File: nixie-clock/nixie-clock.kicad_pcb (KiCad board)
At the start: 2 copper layers, 184 x 105 mm, 61 parts, among them J1 Barrel_Jack_Switch, J2 Conn_01x08, J3 Conn_01x06, J4 AVR-ISP-6, SW1 SW_Push, SW2 SW_Push, SW3 SW_Push, SW4 SW_Push, U1 NCH6100HV, U10 74HC595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

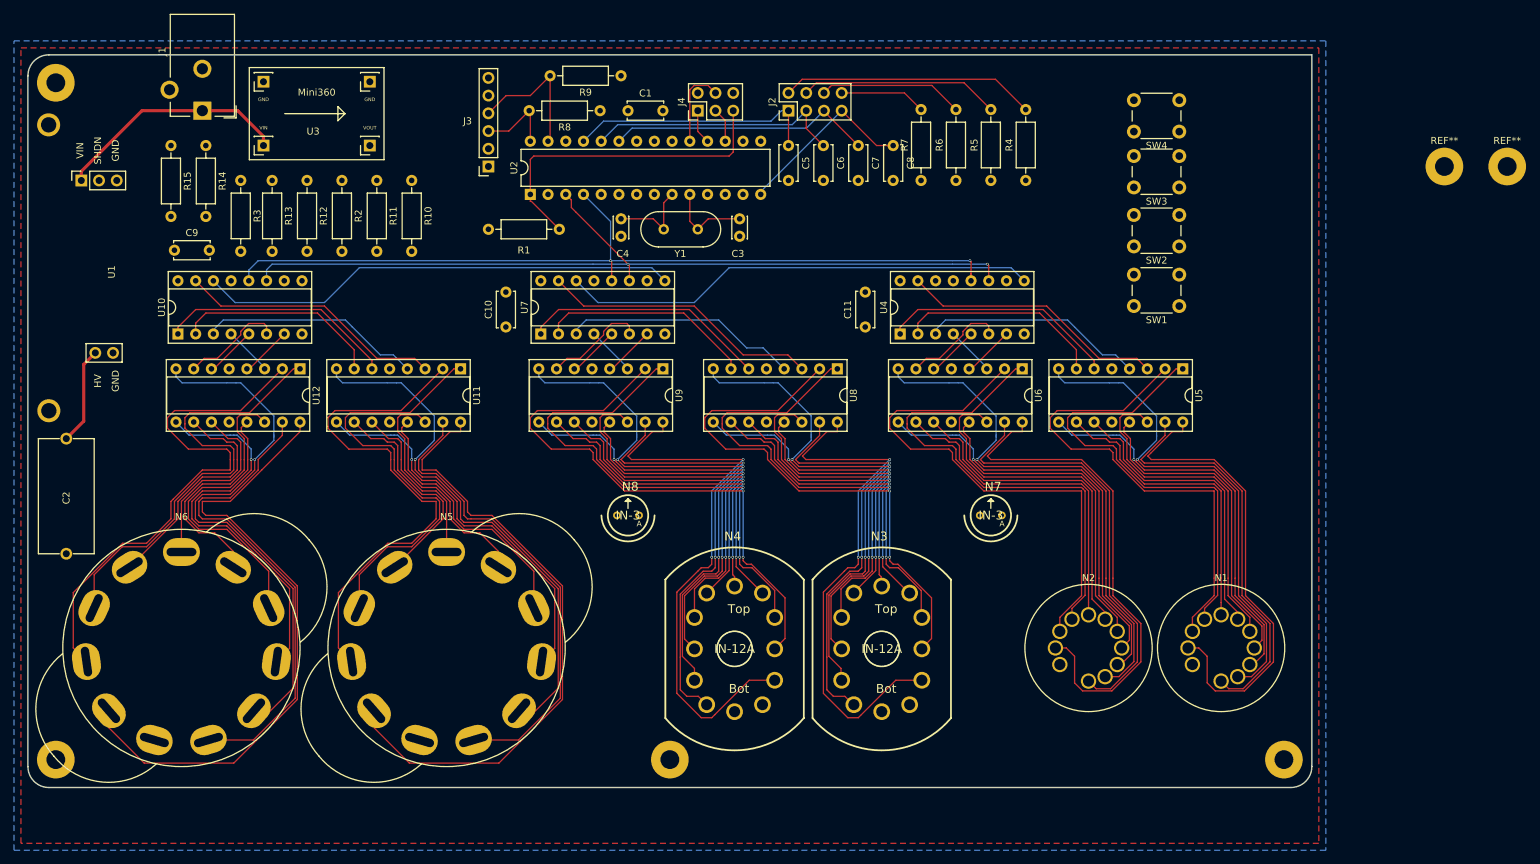
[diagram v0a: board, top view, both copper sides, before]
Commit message: Fixed anode net names. Finished routing anode connections.
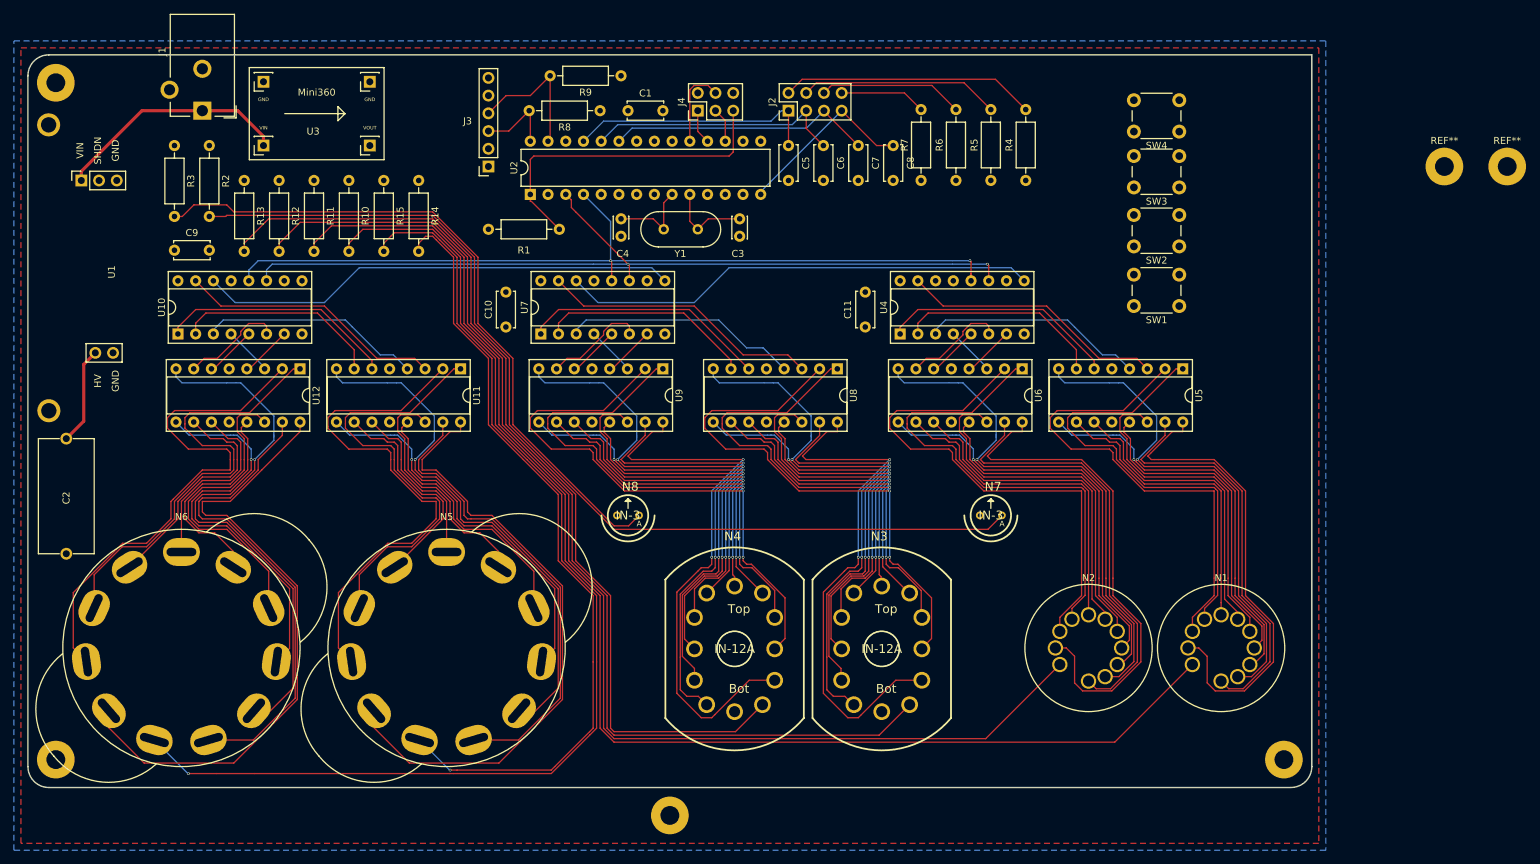
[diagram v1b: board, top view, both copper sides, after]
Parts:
- moved R14 30.9 mm to (84.0, 48.0)
- moved R15 30.9 mm to (79.0, 48.0)
- moved R2 19.6 mm to (54.0, 43.0)
- moved R3 10.7 mm to (49.0, 43.0)
- moved R10 9.00 mm to (74.0, 48.0)
- moved R11 9.00 mm to (69.0, 48.0)
- moved REF** 8.00 mm to (120.0, 139.0)
- moved R12 4.00 mm to (64.0, 48.0)
- moved R13 4.00 mm to (59.0, 48.0)
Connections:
- net Net-(N1-PadA) renamed /shiftout/AnodeN1
- net Net-(N2-PadA) renamed /shiftout/AnodeN2
- net Net-(N3-PadA) renamed /shiftout/AnodeN3
- net Net-(N4-PadA) renamed /shiftout/AnodeN4
- net Net-(N5-PadA) renamed /shiftout/AnodeN5
- net Net-(N6-PadA) renamed /shiftout/AnodeN6
- net Net-(N7-PadA) renamed /AnodeN7
- net Net-(N8-PadA) renamed /AnodeN8
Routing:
- net /shiftout/AnodeN1: track 0.00 -> 185.8 mm
- net /shiftout/AnodeN2: track 0.00 -> 171.8 mm
- net /shiftout/AnodeN6: track 0.00 -> 157.5 mm, vias 0 -> 1
- net /shiftout/AnodeN3: track 0.00 -> 152.8 mm
- net /AnodeN7: track 0.00 -> 144.3 mm
- net /shiftout/AnodeN4: track 0.00 -> 136.8 mm
- net /shiftout/AnodeN5: track 0.00 -> 112.7 mm, vias 0 -> 1
- net /AnodeN8: track 0.00 -> 98.1 mm

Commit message: Finished front silkscreen, added warning symbol, finished edge rounding and mounting holes. Need to add back silkscreen info and run DRC.
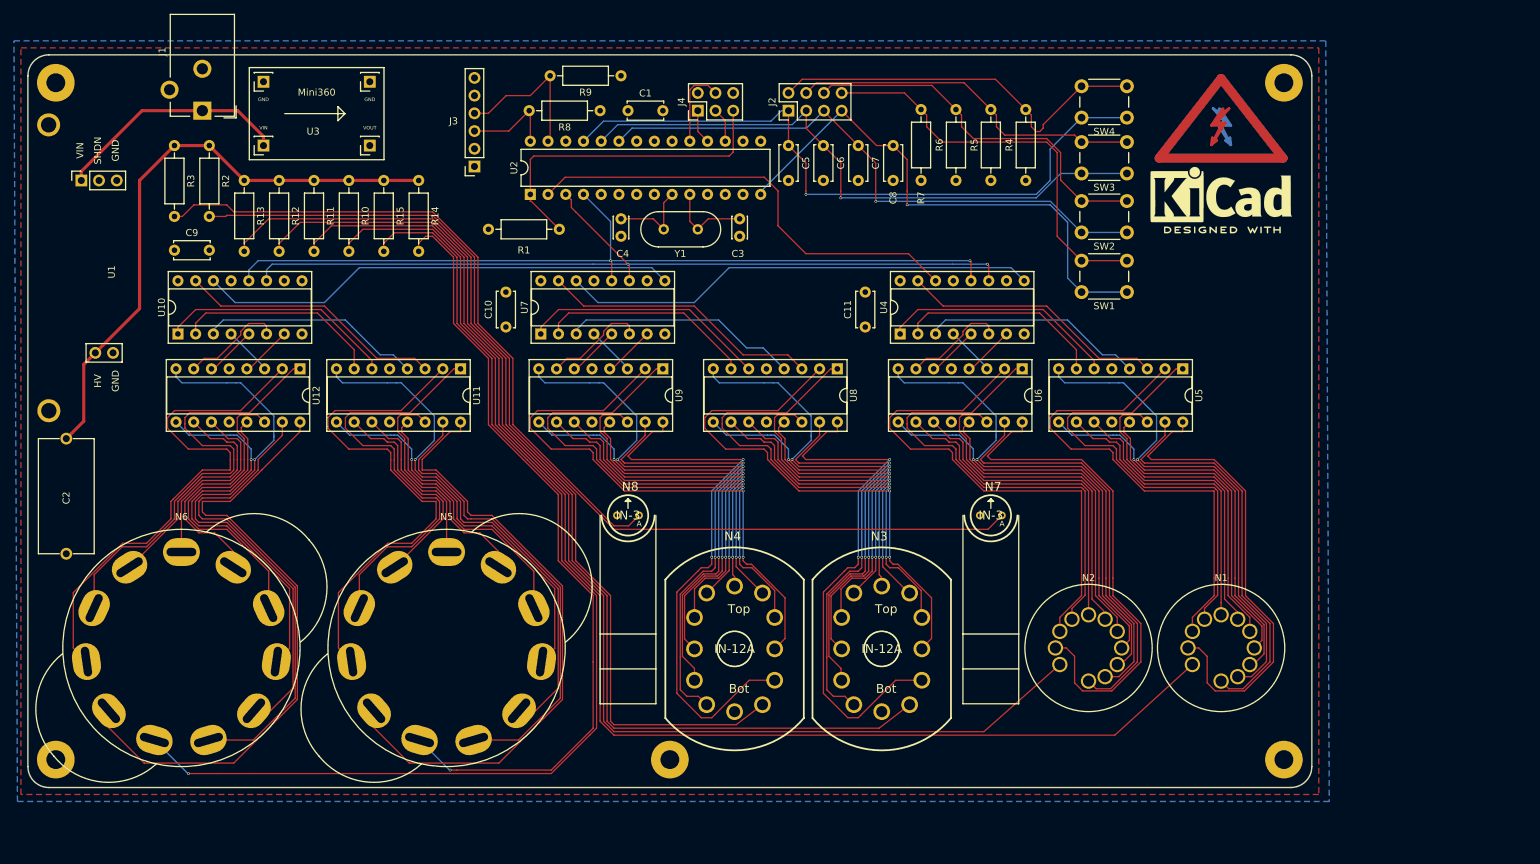
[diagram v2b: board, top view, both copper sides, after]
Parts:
- removed the REF** at (231.0, 46.0)
- removed the REF** at (240.0, 46.0)
- removed the REF** at (120.0, 139.0)
- added REF**: Symbol_Highvoltage_Type2_CopperTop_Small, Symbol:Symbol_Highvoltage_Type2_CopperTop_Small, B.Cu at (199.0, 41.0)
- added REF**: KiCad-Logo2_8mm_SilkScreen, Symbol:KiCad-Logo2_8mm_SilkScreen, F.Cu at (199.0, 50.0)
- added REF**: Symbol_Highvoltage_Type2_CopperTop_Small, Symbol:Symbol_Highvoltage_Type2_CopperTop_Small, F.Cu at (199.0, 41.0)
- added REF**: MountingHole_2.7mm_M2.5_Pad, MountingHole:MountingHole_2.7mm_M2.5_Pad, F.Cu at (208.0, 34.0)
- added REF**: MountingHole_2.7mm_M2.5_Pad, MountingHole:MountingHole_2.7mm_M2.5_Pad, F.Cu at (120.0, 131.0)
- moved SW1 7.76 mm to (185.5, 64.0)
- moved SW2 7.76 mm to (185.5, 55.5)
- moved SW3 7.76 mm to (185.5, 47.0)
- moved SW4 7.76 mm to (185.5, 39.0)
- moved J3 2.00 mm to (92.0, 46.0)
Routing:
- net +170V: track 14.0 -> 85.5 mm
- net SRDATA: track 0.00 -> 65.6 mm
- net pb_programming_select: track 36.2 -> 97.4 mm, vias 0 -> 1
- net pb_minus: track 37.2 -> 88.2 mm, vias 0 -> 1
- net pb_display_on: track 26.3 -> 76.9 mm, vias 0 -> 1
- net pb_plus: track 38.2 -> 85.1 mm, vias 0 -> 1
- net Net-(J2-Pad8): track 12.4 -> 58.8 mm
- net Net-(J2-Pad6): track 20.8 -> 54.0 mm
- net Net-(J2-Pad4): track 28.7 -> 51.1 mm
- net Net-(J2-Pad2): track 36.6 -> 56.4 mm
- net SDA: track 20.6 -> 22.6 mm
- net SCL: track 11.5 -> 13.5 mm
- net /shiftout/AnodeN2: track 171.8 -> 170.0 mm
- net /shiftout/AnodeN1: track 185.8 -> 184.1 mm
- net /shiftout/AnodeN3: track 152.8 -> 151.2 mm
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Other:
- outline, holes or cut-outs redrawn
- board text removed: "Anodes for all nixies Cross SR connections Extra pushbuttons Pushbutton mounting board Final board shape Extras (margins, info, symbols) on silkscreen"

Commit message: Added back silkscreen. Ready for DRC.
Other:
- board text added: "+5V"
- board text added: "IN1, IN12, IN2, IN3 Nixie Clock Nathan Aquino Dornback April 24th, 2020"
- board text added: "ISP"
- board text added: "NCH6100HV"
- board text added: "Pushbutton Board"
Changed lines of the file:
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@@
   (general
     (thickness 1.6)
-    (drawings 52)
+    (drawings 65)
     (tracks 1456)
     (zones 0)
@@
     (38 B.Mask user)
     (39 F.Mask user)
-    (40 Dwgs.User user)
-    (41 Cmts.User user)
+    (40 Dwgs.User user hide)
+    (41 Cmts.User user hide)
     (42 Eco1.User user)
     (43 Eco2.User user)
@@
     (descr "Through hole straight socket strip, 1x06, 2.54mm pitch, single row (from Kicad 4.0.7), script generated")
     (tags "Through hole socket strip THT 1x06 2.54mm single row")
-    (fp_text reference J3 (at 3 6.5) (layer F.SilkS)
+    (fp_text reference J3 (at 0 -3) (layer F.SilkS)
       (effects (font (size 1 1) (thickness 0.15)))
     )
@@
     )
   )
+  (gr_text NCH6100HV (at 34 61 90) (layer F.SilkS)
+    (effects (font (size 1 1) (thickness 0.15)))
+  )
+  (gr_text "Pushbutton Board" (at 141 32) (layer F.SilkS)
+    (effects (font (size 1 1) (thickness 0.15)))
+  )
+  (gr_text ISP (at 127 32) (layer F.SilkS)
+    (effects (font (size 1 1) (thickness 0.15)))
+  )
+  (dimension 89 (width 0.12) (layer B.SilkS)
+    (gr_text "97.000 mm" (at 206.73 82.5 90) (layer B.SilkS)
+      (effects (font (size 1 1) (thickness 0.15)))
+    )
+    (feature1 (pts (xy 210 38) (xy 207.413579 38)))
+    (feature2 (pts (xy 210 127) (xy 207.413579 127)))
+    (crossbar (pts (xy 208 127) (xy 208 38)))
+    (arrow1a (pts (xy 208 38) (xy 208.586421 39.126504)))
+    (arrow1b (pts (xy 208 38) (xy 207.413579 39.126504)))
+    (arrow2a (pts (xy 208 127) (xy 208.586421 125.873496)))
+    (arrow2b (pts (xy 208 127) (xy 207.413579 125.873496)))
+  )
+  (dimension 80 (width 0.12) (layer B.SilkS)
+    (gr_text "88.000 mm" (at 76 129.73) (layer B.SilkS)
+      (effects (font (size 1 1) (thickness 0.15)) (justify mirror))
+    )
+    (feature1 (pts (xy 116 133) (xy 116 130.413579)))
+    (feature2 (pts (xy 36 133) (xy 36 130.413579)))
+    (crossbar (pts (xy 36 131) (xy 116 131)))
+    (arrow1a (pts (xy 116 131) (xy 114.873496 131.586421)))
+    (arrow1b (pts (xy 116 131) (xy 114.873496 130.413579)))
+    (arrow2a (pts (xy 36 131) (xy 37.126504 131.586421)))
+    (arrow2b (pts (xy 36 131) (xy 37.126504 130.413579)))
+  )
+  (dimension 80 (width 0.12) (layer B.SilkS)
+    (gr_text "88.000 mm" (at 164 129.73) (layer B.SilkS)
+      (effects (font (size 1 1) (thickness 0.15)) (justify mirror))
+    )
+    (feature1 (pts (xy 204 133) (xy 204 130.413579)))
+    (feature2 (pts (xy 124 133) (xy 124 130.413579)))
+    (crossbar (pts (xy 124 131) (xy 204 131)))
+    (arrow1a (pts (xy 204 131) (xy 202.873496 131.586421)))
+    (arrow1b (pts (xy 204 131) (xy 202.873496 130.413579)))
+    (arrow2a (pts (xy 124 131) (xy 125.126504 131.586421)))
+    (arrow2b (pts (xy 124 131) (xy 125.126504 130.413579)))
+  )
+  (gr_text "IN1, IN12, IN2, IN3 Nixie Clock\nNathan Aquino Dornback\nApril 24th, 2020" (at 203 126) (layer B.SilkS)
+    (effects (font (size 1 1) (thickness 0.15)) (justify left mirror))
+  )
+  (gr_text +5V (at 88 36) (layer F.SilkS)
+    (effects (font (size 1 1) (thickness 0.15)))
+  )
+  (gr_line (start 88.6 40.2) (end 88.1 39.7) (layer F.SilkS) (width 0.12))
+  (gr_line (start 88.6 39.2) (end 88.6 40.2) (layer F.SilkS) (width 0.12))
+  (gr_line (start 88.1 39.7) (end 88.6 39.2) (layer F.SilkS) (width 0.12))
+  (gr_line (start 89.6 39.7) (end 88.1 39.7) (layer F.SilkS) (width 0.12))
+  (gr_circle (center 85 133.5) (end 85 133.5) (layer F.SilkS) (width 0.5))
   (gr_circle (center 99 70) (end 99 70) (layer F.SilkS) (width 0.5))
   (gr_circle (center 150.5 70) (end 150.5 70) (layer F.SilkS) (width 0.5))
@@
   (gr_circle (center 156 124.5) (end 156 124.5) (layer F.SilkS) (width 0.5))
   (gr_circle (center 135 124.5) (end 135 124.5) (layer F.SilkS) (width 0.5))
-  (gr_circle (center 46.5 133) (end 46.5 133) (layer F.SilkS) (width 0.5))
+  (gr_circle (center 46.5 133.5) (end 46.5 133.5) (layer F.SilkS) (width 0.5))
   (gr_circle (center 196 75) (end 196 75) (layer F.SilkS) (width 0.5))
   (gr_circle (center 173 75) (end 173 75) (layer F.SilkS) (width 0.5))
